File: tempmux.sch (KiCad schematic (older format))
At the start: 23 parts, among them J3 Conn_02x07_Counter_Clockwise, U11 CD74HC4067SM

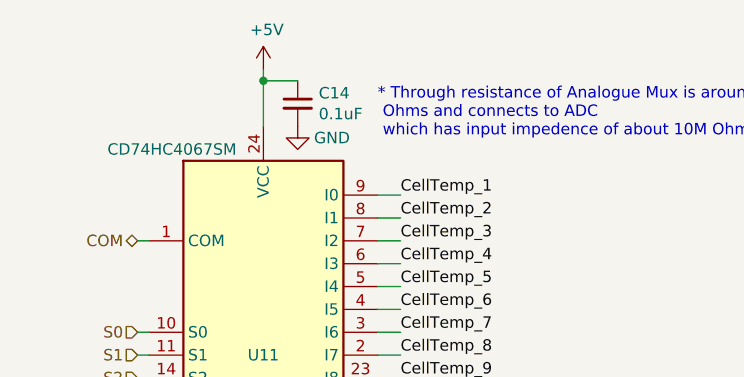
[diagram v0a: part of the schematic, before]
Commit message: Removed SD card Adapter, added programming port
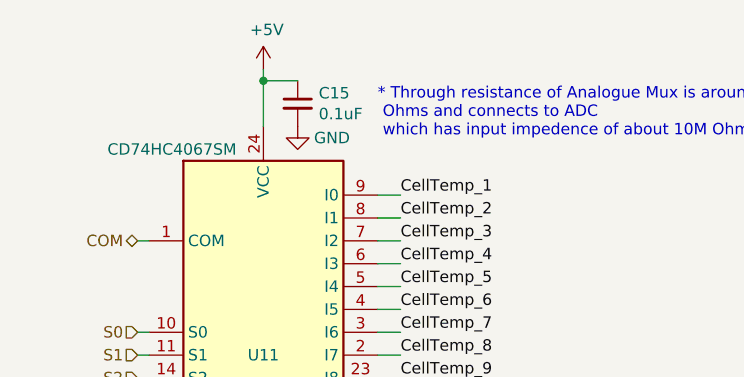
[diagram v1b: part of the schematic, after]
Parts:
- renumbered C14 to C15
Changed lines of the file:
@@
 P 2150 1100
 AR Path="/5F70A721/5F6868E0" Ref="C?"  Part="1"
-AR Path="/5F70B1A3/5F6868E0" Ref="C14"  Part="1"
-F 0 "C14" H 2242 1146 50  0000 L CNN
+AR Path="/5F70B1A3/5F6868E0" Ref="C15"  Part="1"
+F 0 "C15" H 2242 1146 50  0000 L CNN
 F 1 "0.1uF" H 2242 1055 50  0000 L CNN
 F 2 "Capacitor_SMD:C_1206_3216Metric" H 2150 1100 50  0001 C CNN

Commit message: Added ext ADC pin and fixed connection bugs
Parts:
- renumbered J3 to J7
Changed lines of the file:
@@
 P 2000 3400
 AR Path="/5F70A721/5F6868D9" Ref="#PWR?"  Part="1"
-AR Path="/5F70B1A3/5F6868D9" Ref="#PWR077"  Part="1"
-F 0 "#PWR077" H 2000 3150 50  0001 C CNN
+AR Path="/5F70B1A3/5F6868D9" Ref="#PWR079"  Part="1"
+F 0 "#PWR079" H 2000 3150 50  0001 C CNN
 F 1 "GND" H 2005 3227 50  0000 C CNN
 F 2 "" H 2000 3400 50  0001 C CNN
@@
 P 2150 1200
 AR Path="/5F70A721/5F6868E6" Ref="#PWR?"  Part="1"
-AR Path="/5F70B1A3/5F6868E6" Ref="#PWR062"  Part="1"
-F 0 "#PWR062" H 2150 950 50  0001 C CNN
+AR Path="/5F70B1A3/5F6868E6" Ref="#PWR064"  Part="1"
+F 0 "#PWR064" H 2150 950 50  0001 C CNN
 F 1 "GND" H 2300 1150 50  0000 C CNN
 F 2 "" H 2150 1200 50  0001 C CNN
@@
 P 2000 950
 AR Path="/5F70A721/5F6868EC" Ref="#PWR?"  Part="1"
-AR Path="/5F70B1A3/5F6868EC" Ref="#PWR061"  Part="1"
-F 0 "#PWR061" H 2000 800 50  0001 C CNN
+AR Path="/5F70B1A3/5F6868EC" Ref="#PWR063"  Part="1"
+F 0 "#PWR063" H 2000 800 50  0001 C CNN
 F 1 "+5V" H 2015 1123 50  0000 C CNN
 F 2 "" H 2000 950 50  0001 C CNN
@@
 P 9900 1850
 AR Path="/5F70A721/5F68B135" Ref="J?"  Part="1"
-AR Path="/5F70B1A3/5F68B135" Ref="J3"  Part="1"
-F 0 "J3" H 9950 2300 50  0000 C CNN
+AR Path="/5F70B1A3/5F68B135" Ref="J7"  Part="1"
+F 0 "J7" H 9950 2300 50  0000 C CNN
 F 1 "Conn_02x07_Counter_Clockwise" H 9950 1450 50  0000 C CNN
 F 2 "Connector_PinHeader_2.54mm:PinHeader_2x07_P2.54mm_Vertical" H 9900 1850 50  0001 C CNN
@@
 P 9650 1550
 AR Path="/5F70A721/5F68DF75" Ref="#PWR?"  Part="1"
-AR Path="/5F70B1A3/5F68DF75" Ref="#PWR063"  Part="1"
-F 0 "#PWR063" H 9650 1400 50  0001 C CNN
+AR Path="/5F70B1A3/5F68DF75" Ref="#PWR065"  Part="1"
+F 0 "#PWR065" H 9650 1400 50  0001 C CNN
 F 1 "+5V" H 9665 1723 50  0000 C CNN
 F 2 "" H 9650 1550 50  0001 C CNN
@@
 P 10250 1550
 AR Path="/5F70A721/5F68E7C7" Ref="#PWR?"  Part="1"
-AR Path="/5F70B1A3/5F68E7C7" Ref="#PWR064"  Part="1"
-F 0 "#PWR064" H 10250 1400 50  0001 C CNN
+AR Path="/5F70B1A3/5F68E7C7" Ref="#PWR066"  Part="1"
+F 0 "#PWR066" H 10250 1400 50  0001 C CNN
 F 1 "+5V" H 10265 1723 50  0000 C CNN
 F 2 "" H 10250 1550 50  0001 C CNN
@@
 P 5000 1800
 AR Path="/5F70A721/5F6A4A53" Ref="#PWR?"  Part="1"
-AR Path="/5F70B1A3/5F6A4A53" Ref="#PWR065"  Part="1"
-F 0 "#PWR065" H 5000 1550 50  0001 C CNN
+AR Path="/5F70B1A3/5F6A4A53" Ref="#PWR067"  Part="1"
+F 0 "#PWR067" H 5000 1550 50  0001 C CNN
 F 1 "GND" H 5005 1627 50  0000 C CNN
 F 2 "" H 5000 1800 50  0001 C CNN
@@
 P 5500 1800
 AR Path="/5F70A721/5F6A4F23" Ref="#PWR?"  Part="1"
-AR Path="/5F70B1A3/5F6A4F23" Ref="#PWR066"  Part="1"
-F 0 "#PWR066" H 5500 1550 50  0001 C CNN
+AR Path="/5F70B1A3/5F6A4F23" Ref="#PWR068"  Part="1"
+F 0 "#PWR068" H 5500 1550 50  0001 C CNN
 F 1 "GND" H 5505 1627 50  0000 C CNN
 F 2 "" H 5500 1800 50  0001 C CNN
@@
 P 6000 1800
 AR Path="/5F70A721/5F6A5197" Ref="#PWR?"  Part="1"
-AR Path="/5F70B1A3/5F6A5197" Ref="#PWR067"  Part="1"
-F 0 "#PWR067" H 6000 1550 50  0001 C CNN
+AR Path="/5F70B1A3/5F6A5197" Ref="#PWR069"  Part="1"
+F 0 "#PWR069" H 6000 1550 50  0001 C CNN
 F 1 "GND" H 6005 1627 50  0000 C CNN
 F 2 "" H 6000 1800 50  0001 C CNN
@@
 P 6500 1800
 AR Path="/5F70A721/5F6A5348" Ref="#PWR?"  Part="1"
-AR Path="/5F70B1A3/5F6A5348" Ref="#PWR068"  Part="1"
-F 0 "#PWR068" H 6500 1550 50  0001 C CNN
+AR Path="/5F70B1A3/5F6A5348" Ref="#PWR070"  Part="1"
+F 0 "#PWR070" H 6500 1550 50  0001 C CNN
 F 1 "GND" H 6505 1627 50  0000 C CNN
 F 2 "" H 6500 1800 50  0001 C CNN
@@
 P 7000 1800
 AR Path="/5F70A721/5F6A55E5" Ref="#PWR?"  Part="1"
-AR Path="/5F70B1A3/5F6A55E5" Ref="#PWR069"  Part="1"
-F 0 "#PWR069" H 7000 1550 50  0001 C CNN
+AR Path="/5F70B1A3/5F6A55E5" Ref="#PWR071"  Part="1"
+F 0 "#PWR071" H 7000 1550 50  0001 C CNN
 F 1 "GND" H 7005 1627 50  0000 C CNN
 F 2 "" H 7000 1800 50  0001 C CNN
@@
 P 7500 1800
 AR Path="/5F70A721/5F6A585F" Ref="#PWR?"  Part="1"
-AR Path="/5F70B1A3/5F6A585F" Ref="#PWR070"  Part="1"
-F 0 "#PWR070" H 7500 1550 50  0001 C CNN
+AR Path="/5F70B1A3/5F6A585F" Ref="#PWR072"  Part="1"
+F 0 "#PWR072" H 7500 1550 50  0001 C CNN
 F 1 "GND" H 7505 1627 50  0000 C CNN
 F 2 "" H 7500 1800 50  0001 C CNN
@@
 P 5000 3050
 AR Path="/5F70A721/5F6A59FF" Ref="#PWR?"  Part="1"
-AR Path="/5F70B1A3/5F6A59FF" Ref="#PWR071"  Part="1"
-F 0 "#PWR071" H 5000 2800 50  0001 C CNN
+AR Path="/5F70B1A3/5F6A59FF" Ref="#PWR073"  Part="1"
+F 0 "#PWR073" H 5000 2800 50  0001 C CNN
 F 1 "GND" H 5005 2877 50  0000 C CNN
 F 2 "" H 5000 3050 50  0001 C CNN
@@
 P 5500 3050
 AR Path="/5F70A721/5F6A5CE6" Ref="#PWR?"  Part="1"
-AR Path="/5F70B1A3/5F6A5CE6" Ref="#PWR072"  Part="1"
-F 0 "#PWR072" H 5500 2800 50  0001 C CNN
+AR Path="/5F70B1A3/5F6A5CE6" Ref="#PWR074"  Part="1"
+F 0 "#PWR074" H 5500 2800 50  0001 C CNN
 F 1 "GND" H 5505 2877 50  0000 C CNN
 F 2 "" H 5500 3050 50  0001 C CNN
@@
 P 6000 3050
 AR Path="/5F70A721/5F6A5EEC" Ref="#PWR?"  Part="1"
-AR Path="/5F70B1A3/5F6A5EEC" Ref="#PWR073"  Part="1"
-F 0 "#PWR073" H 6000 2800 50  0001 C CNN
+AR Path="/5F70B1A3/5F6A5EEC" Ref="#PWR075"  Part="1"
+F 0 "#PWR075" H 6000 2800 50  0001 C CNN
 F 1 "GND" H 6005 2877 50  0000 C CNN
 F 2 "" H 6000 3050 50  0001 C CNN
@@
 P 6500 3050
 AR Path="/5F70A721/5F6A6093" Ref="#PWR?"  Part="1"
-AR Path="/5F70B1A3/5F6A6093" Ref="#PWR074"  Part="1"
-F 0 "#PWR074" H 6500 2800 50  0001 C CNN
+AR Path="/5F70B1A3/5F6A6093" Ref="#PWR076"  Part="1"
+F 0 "#PWR076" H 6500 2800 50  0001 C CNN
 F 1 "GND" H 6505 2877 50  0000 C CNN
 F 2 "" H 6500 3050 50  0001 C CNN
@@
 P 7000 3050
 AR Path="/5F70A721/5F6A622C" Ref="#PWR?"  Part="1"
-AR Path="/5F70B1A3/5F6A622C" Ref="#PWR075"  Part="1"
-F 0 "#PWR075" H 7000 2800 50  0001 C CNN
+AR Path="/5F70B1A3/5F6A622C" Ref="#PWR077"  Part="1"
+F 0 "#PWR077" H 7000 2800 50  0001 C CNN
 F 1 "GND" H 7005 2877 50  0000 C CNN
 F 2 "" H 7000 3050 50  0001 C CNN
@@
 P 7500 3050
 AR Path="/5F70A721/5F6A6421" Ref="#PWR?"  Part="1"
-AR Path="/5F70B1A3/5F6A6421" Ref="#PWR076"  Part="1"
-F 0 "#PWR076" H 7500 2800 50  0001 C CNN
+AR Path="/5F70B1A3/5F6A6421" Ref="#PWR078"  Part="1"
+F 0 "#PWR078" H 7500 2800 50  0001 C CNN
 F 1 "GND" H 7505 2877 50  0000 C CNN
 F 2 "" H 7500 3050 50  0001 C CNN
@@
 P 5000 4450
 AR Path="/5F70A721/5F26879D" Ref="#PWR?"  Part="1"
-AR Path="/5F70B1A3/5F26879D" Ref="#PWR082"  Part="1"
-F 0 "#PWR082" H 5000 4200 50  0001 C CNN
+AR Path="/5F70B1A3/5F26879D" Ref="#PWR084"  Part="1"
+F 0 "#PWR084" H 5000 4200 50  0001 C CNN
 F 1 "GND" H 5005 4277 50  0000 C CNN
 F 2 "" H 5000 4450 50  0001 C CNN
@@
 P 5000 3650
 AR Path="/5F70A721/5F269BD4" Ref="#PWR?"  Part="1"
-AR Path="/5F70B1A3/5F269BD4" Ref="#PWR078"  Part="1"
-F 0 "#PWR078" H 5000 3500 50  0001 C CNN
+AR Path="/5F70B1A3/5F269BD4" Ref="#PWR080"  Part="1"
+F 0 "#PWR080" H 5000 3500 50  0001 C CNN
 F 1 "+5V" H 5015 3823 50  0000 C CNN
 F 2 "" H 5000 3650 50  0001 C CNN
@@
 P 6000 4450
 AR Path="/5F70A721/5F26E1A4" Ref="#PWR?"  Part="1"
-AR Path="/5F70B1A3/5F26E1A4" Ref="#PWR083"  Part="1"
-F 0 "#PWR083" H 6000 4200 50  0001 C CNN
+AR Path="/5F70B1A3/5F26E1A4" Ref="#PWR085"  Part="1"
+F 0 "#PWR085" H 6000 4200 50  0001 C CNN
 F 1 "GND" H 6005 4277 50  0000 C CNN
 F 2 "" H 6000 4450 50  0001 C CNN
@@
 P 6000 3650
 AR Path="/5F70A721/5F26E1AB" Ref="#PWR?"  Part="1"
-AR Path="/5F70B1A3/5F26E1AB" Ref="#PWR079"  Part="1"
-F 0 "#PWR079" H 6000 3500 50  0001 C CNN
+AR Path="/5F70B1A3/5F26E1AB" Ref="#PWR081"  Part="1"
+F 0 "#PWR081" H 6000 3500 50  0001 C CNN
 F 1 "+5V" H 6015 3823 50  0000 C CNN
 F 2 "" H 6000 3650 50  0001 C CNN
@@
 P 7000 4450
 AR Path="/5F70A721/5F2705CC" Ref="#PWR?"  Part="1"
-AR Path="/5F70B1A3/5F2705CC" Ref="#PWR084"  Part="1"
-F 0 "#PWR084" H 7000 4200 50  0001 C CNN
+AR Path="/5F70B1A3/5F2705CC" Ref="#PWR086"  Part="1"
+F 0 "#PWR086" H 7000 4200 50  0001 C CNN
 F 1 "GND" H 7005 4277 50  0000 C CNN
 F 2 "" H 7000 4450 50  0001 C CNN
@@
 P 7000 3650
 AR Path="/5F70A721/5F2705D3" Ref="#PWR?"  Part="1"
-AR Path="/5F70B1A3/5F2705D3" Ref="#PWR080"  Part="1"
-F 0 "#PWR080" H 7000 3500 50  0001 C CNN
+AR Path="/5F70B1A3/5F2705D3" Ref="#PWR082"  Part="1"
+F 0 "#PWR082" H 7000 3500 50  0001 C CNN
 F 1 "+5V" H 7015 3823 50  0000 C CNN
 F 2 "" H 7000 3650 50  0001 C CNN
@@
 P 8000 4450
 AR Path="/5F70A721/5F272D66" Ref="#PWR?"  Part="1"
-AR Path="/5F70B1A3/5F272D66" Ref="#PWR085"  Part="1"
-F 0 "#PWR085" H 8000 4200 50  0001 C CNN
+AR Path="/5F70B1A3/5F272D66" Ref="#PWR087"  Part="1"
+F 0 "#PWR087" H 8000 4200 50  0001 C CNN
 F 1 "GND" H 8005 4277 50  0000 C CNN
 F 2 "" H 8000 4450 50  0001 C CNN
@@
 P 8000 3650
 AR Path="/5F70A721/5F272D6D" Ref="#PWR?"  Part="1"
-AR Path="/5F70B1A3/5F272D6D" Ref="#PWR081"  Part="1"
-F 0 "#PWR081" H 8000 3500 50  0001 C CNN
+AR Path="/5F70B1A3/5F272D6D" Ref="#PWR083"  Part="1"
+F 0 "#PWR083" H 8000 3500 50  0001 C CNN
 F 1 "+5V" H 8015 3823 50  0000 C CNN
 F 2 "" H 8000 3650 50  0001 C CNN

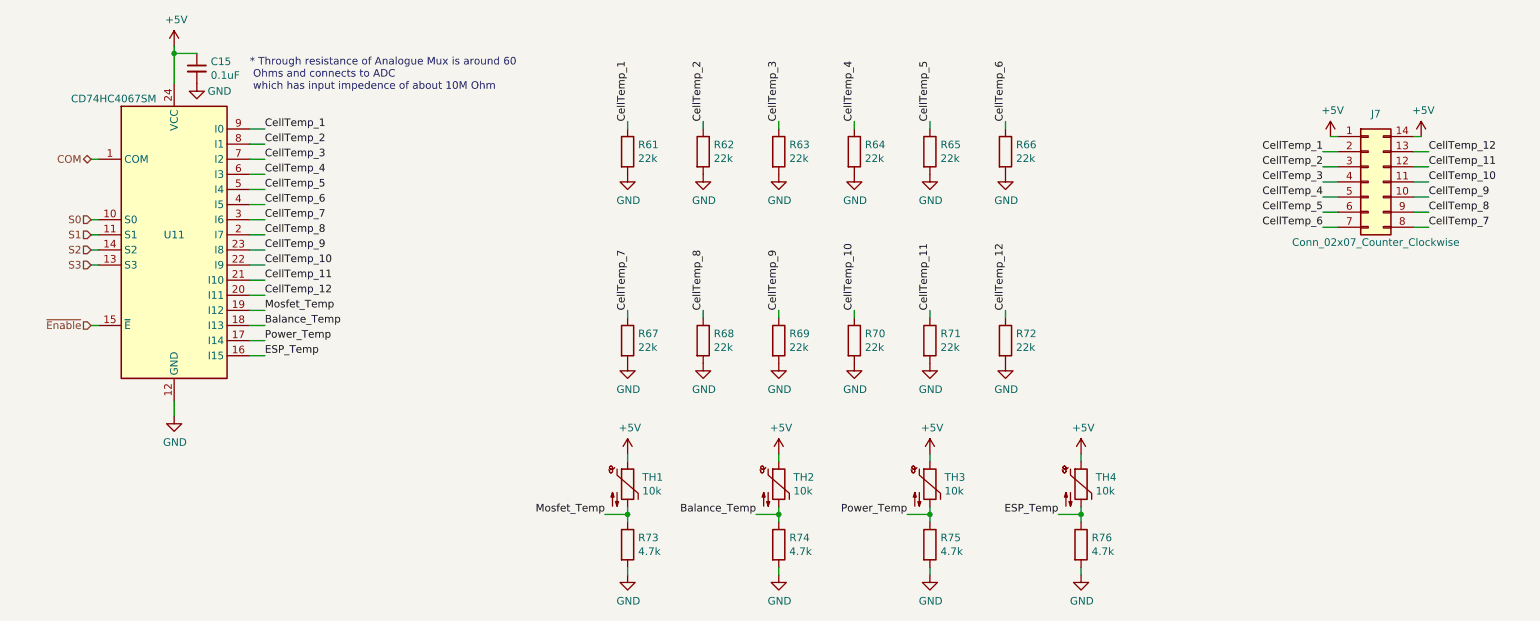
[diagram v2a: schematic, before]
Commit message: Added JST power connect and fixed some footprints
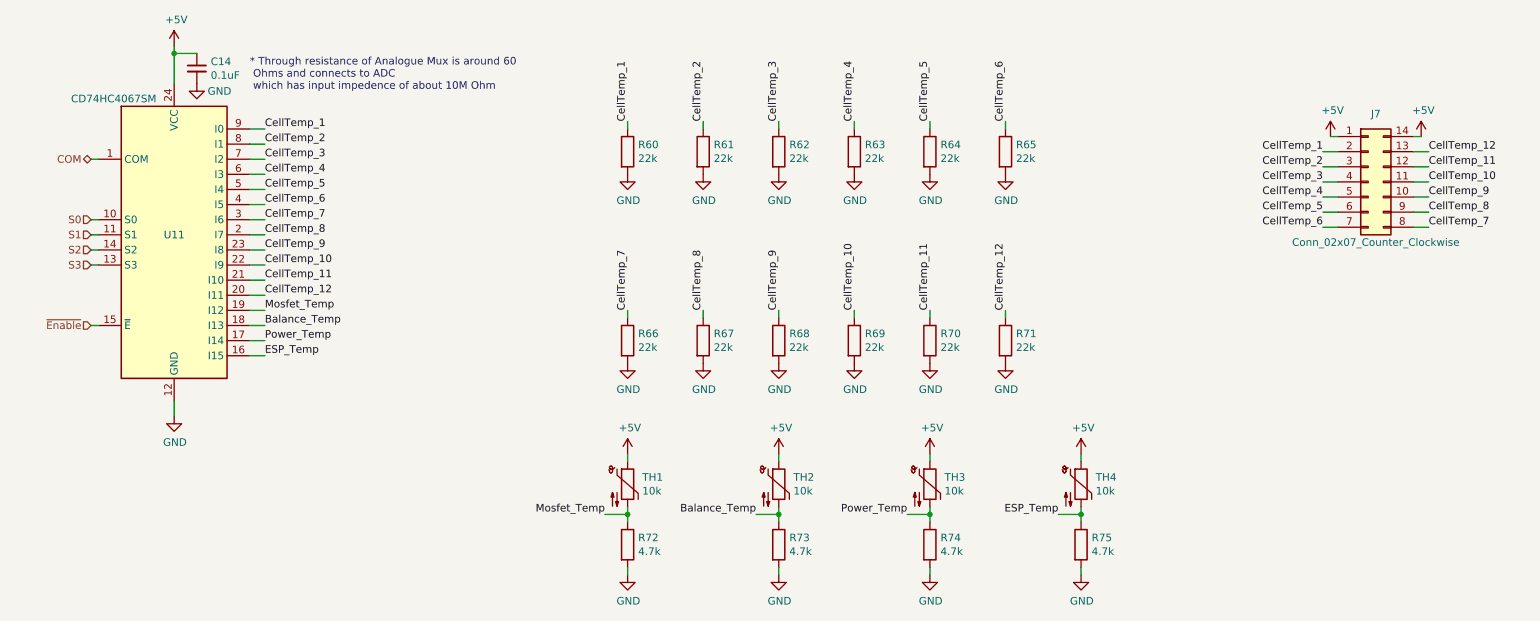
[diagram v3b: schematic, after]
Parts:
- renumbered C15 to C14, R61 to R60, R62 to R61, R63 to R62, R64 to R63, R65 to R64, R66 to R65, R67 to R66, R68 to R67, R69 to R68, R70 to R69, R71 to R70, R72 to R71, R73 to R72, R74 to R73, R75 to R74, R76 to R75
